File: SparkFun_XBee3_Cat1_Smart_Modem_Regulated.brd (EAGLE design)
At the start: 33 x 52.1 mm, 90 parts, among them J4 QWIIC_RIGHT_ANGLE, U2 AP63203

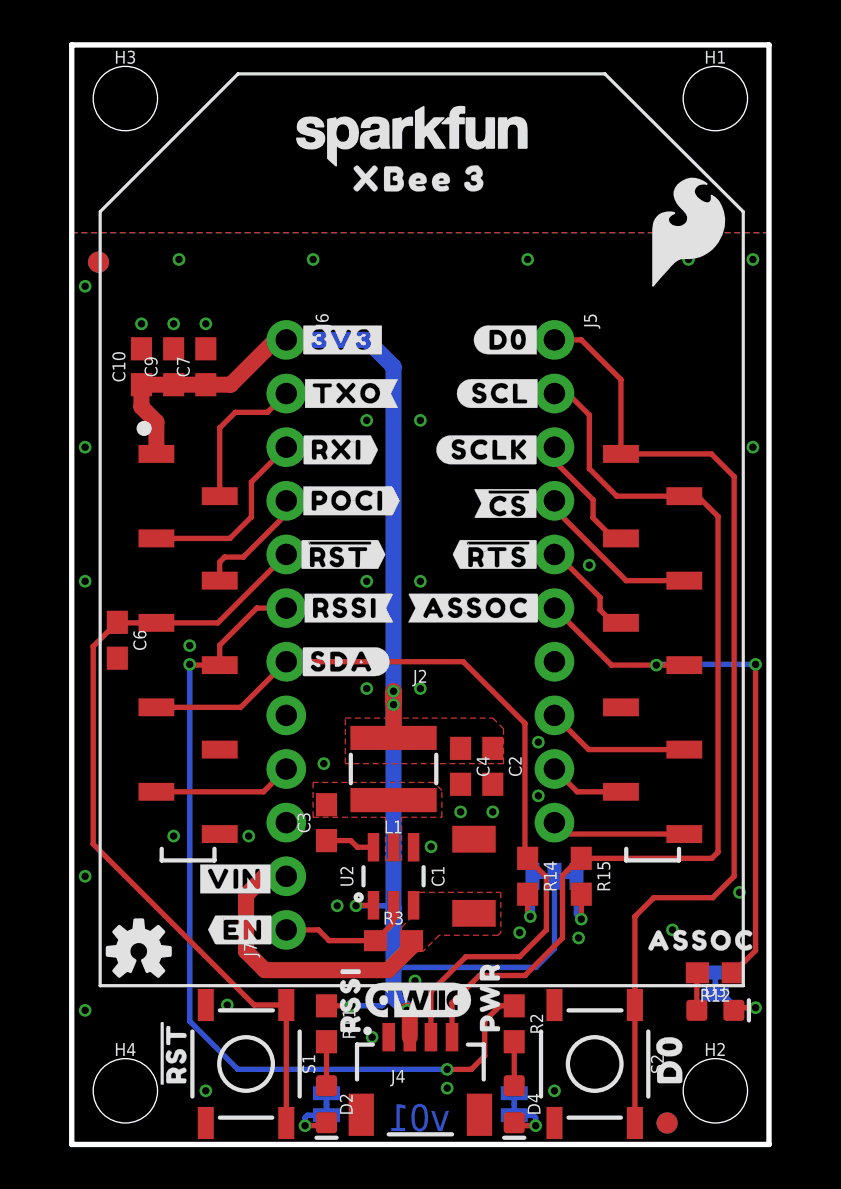
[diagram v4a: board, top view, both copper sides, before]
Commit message: Adds two additional layers, routes all nets, adds most silk
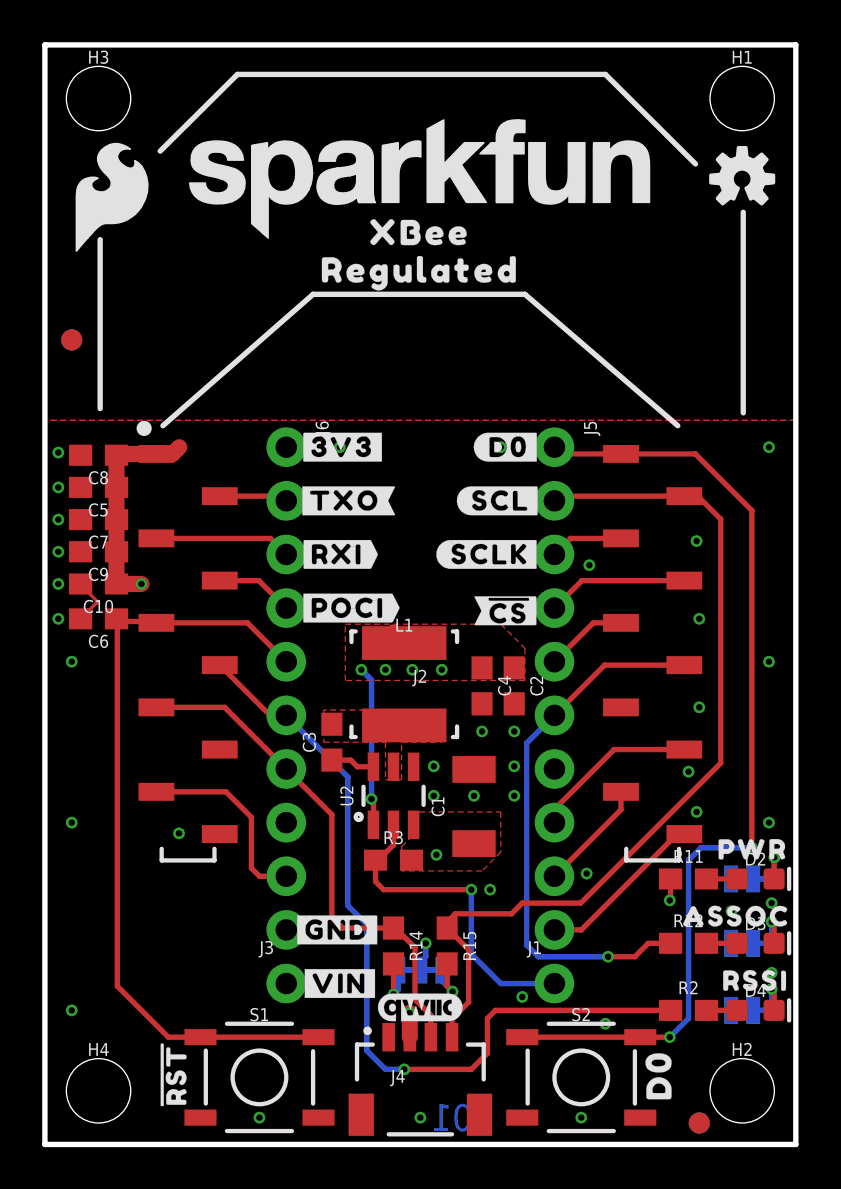
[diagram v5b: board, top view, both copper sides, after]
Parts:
- removed J7: (no value), SparkFun-Connectors:1X02_NO_SILK
- removed LOGO1: SFE_LOGO_NAME.1_INCH, SparkFun-Aesthetics:SFE_LOGO_NAME_.1
- removed U$37: (no value), topmirror:#D7##CTS##26
- removed U$38: (no value), topmirror:#D4#PICO#25
- removed U$48: (no value), topmirror:#EN#17
- removed U$51: (no value), topmirror:#RLED#22
- removed U$53: (no value), top:XBEE_335
- removed U$54: (no value), botmirror:##RST##13
- removed U$55: (no value), topmirror:#RSSI#16
- removed U$56: (no value), botmirror:#SDA#10
- removed U$57: (no value), botmirror:#ASSOC#28
- removed U$58: (no value), botmirror:##RTS##14
- removed U$67: (no value), botmirror:#EN#15
- added C5: 47pF, SparkFun-Capacitors:0603
- added C8: 10pF, SparkFun-Capacitors:0603
- added J1, J3: (no value), SparkFun-Connectors:1X01_NO_SILK_STAND
- added U$1: (no value), topmirror:#GND#0
- added U$10: (no value), top:#D4#PICO#25
- added U$2: (no value), SparkFun-Aesthetics:SFE_LOGO_NAME_.2
- added U$24, U$29: (no value), topmirror:REGULATED1343
- added U$25, U$28: (no value), top:XBEE340
- added U$3: (no value), topmirror:#EN#17
- added U$4: (no value), topmirror:#NC#1
- added U$5: (no value), botmirror:#NC#3
- added U$7: (no value), top:#D7##CTS##26
- D4: value BLUE -> Yellow
- J2: device xbee_smart_modem:XBEE3-SMD_SILK -> xbee_smart_modem:XBEE3-SMD
- L1: value 4.7μH -> 3.9UH; device SparkFun-Coils:INDUCTOR_4X4MM -> SparkFun-Coils:INDUCTOR_3.9UH
- LOGO3: value QWIIC_LOGO_5MM -> QWIIC_LOGO_4MM; device SparkFun-Aesthetics:QWIIC_5MM -> SparkFun-Aesthetics:QWIIC_4MM
- R11: value 1k -> 4.7k
- U$23: device top:XBEE_335 -> top:XBEE340
- moved LOGO2 46.4 mm to (31.8, 45.7)
- moved U$61 27.4 mm to (1.91, 44.8)
- moved D2 23.0 mm to (32.4, 12.6), turned to 0 degrees
- moved PLED 22.4 mm to (31.8, 12.6), turned to 180 degrees
- moved U$52 22.3 mm to (28.3, 12.6)
- moved U$62 19.2 mm to (32.4, 7.75), turned to 0 degrees
- moved R11 18.5 mm to (29.2, 12.6), turned to 0 degrees
- moved FRAME2 14.5 mm to (-10.2, -27.9)
- moved U$42 14.3 mm to (32.3, 14.0), turned to 0 degrees
- moved D4 12.3 mm to (32.4, 6.35), turned to 0 degrees
- moved RLED 11.7 mm to (31.8, 6.35), turned to 180 degrees
- moved C10 10.5 mm to (1.27, 26.5), turned to 180 degrees
- moved C9 9.46 mm to (1.27, 28.1), turned to 180 degrees
- moved C7 8.84 mm to (1.27, 29.6), turned to 180 degrees
- moved R2 8.28 mm to (29.2, 6.35), turned to 0 degrees
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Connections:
- net 3.3V: now also C5.1, C8.1
- net EN: now also J1.1; no longer J7.1
- net GND: now also C5.2, C8.2
- net VIN: now also J3.1; no longer J7.2
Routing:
- net 3.3V: track 69.3 -> 22.3 mm, vias 5 -> 9
- net D11/SDA: track 38.6 -> 24.5 mm
- net EN: track 6.47 -> 15.4 mm, vias 0 -> 1
- net VIN: track 13.9 -> 9.64 mm, vias 0 -> 1
- net D1/SCL: track 46.5 -> 42.7 mm
- net D13/TXO: track 7.06 -> 3.24 mm
- net D10/RSSI_PWM: track 41.7 -> 38.5 mm, vias 2 -> 1
- net D8/!DTR!: track 6.60 -> 9.22 mm
- net D14/RXI: track 8.91 -> 6.46 mm
- net GND: track 0.00 -> 2.41 mm, vias 41 -> 39
- net D2/SPI_CLK: track 5.83 -> 3.46 mm
- net D0: track 47.4 -> 45.5 mm, vias 0 -> 2
- net D7/!CTS!: track 3.60 -> 5.30 mm
- net D4/SPI_PICO: track 6.37 -> 8.03 mm
- net !RESET!: track 38.2 -> 36.8 mm
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- added copper zone on layer 15, net 3.3V
- added copper zone on layer 2, net GND
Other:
- board size 33 x 52.1 mm -> 35.6 x 52.1 mm

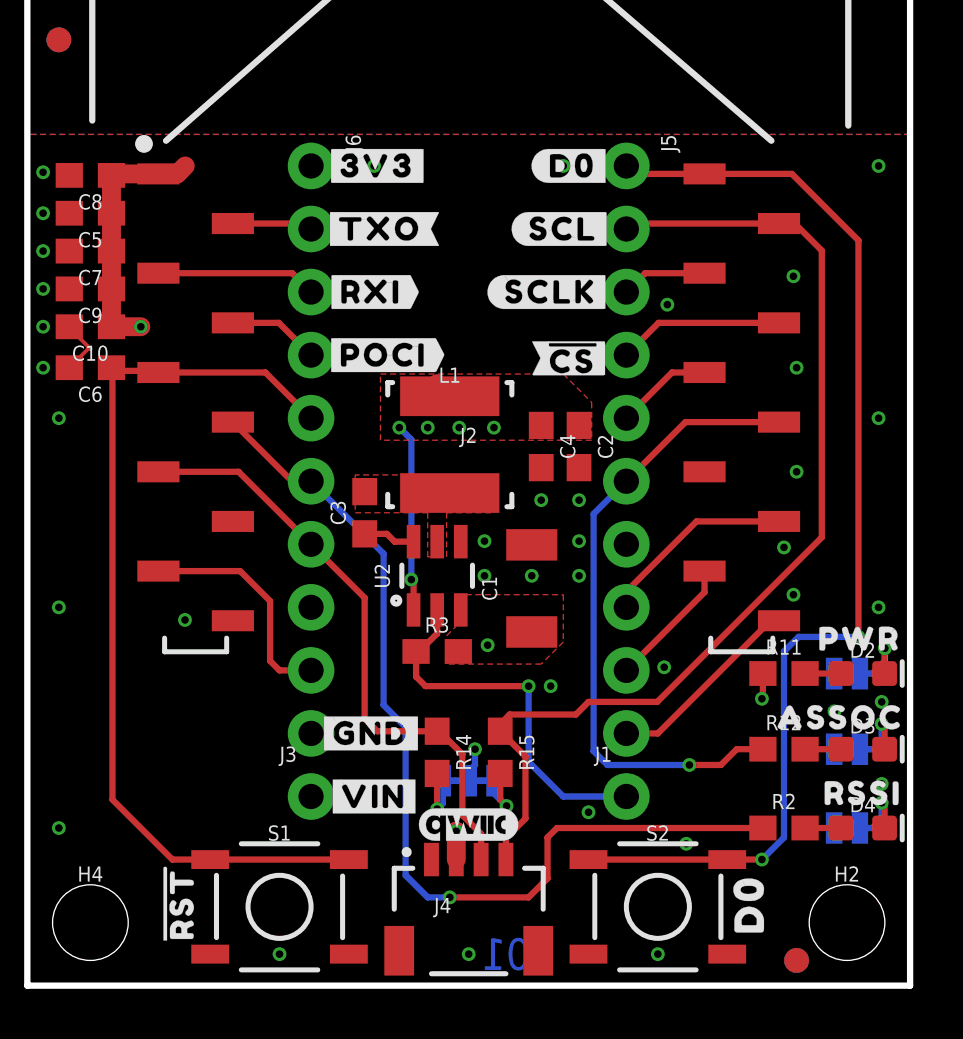
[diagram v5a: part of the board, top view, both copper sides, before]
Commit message: Adds more silk labels,  Adds ordering instructions
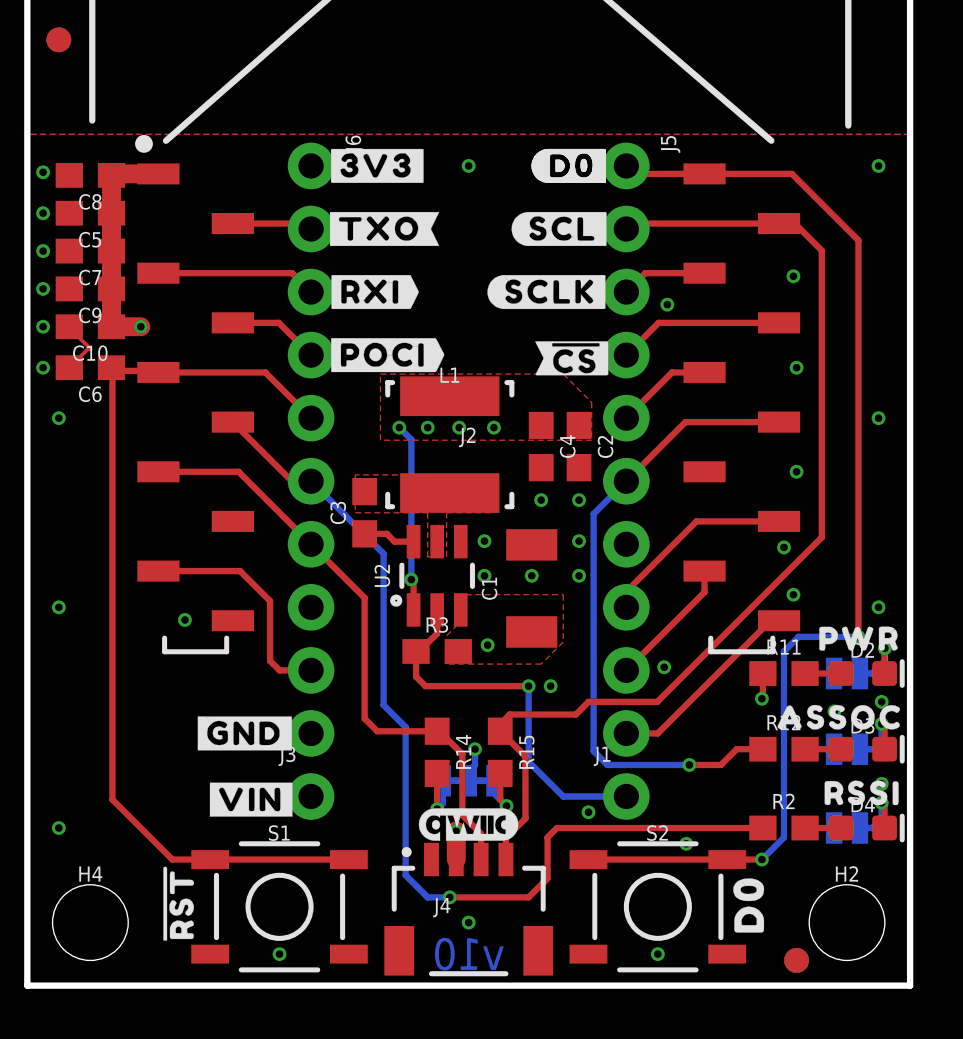
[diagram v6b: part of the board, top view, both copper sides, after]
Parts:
- removed U$6: (no value), topmirror:#D3#AD3#23
- added LOGO1: SPECIAL_INSTRUCTIONS-ORDERING, SparkFun-Aesthetics:ORDERING_INSTRUCTIONS
- added LOGO4: SFE_LOGO_NAMEBLANK, SparkFun-Aesthetics:BLANK
- added U$31: (no value), botmirror:#D0#3
- added U$32: (no value), topmirror:#D1#AD1#SCL#8
- added U$34: (no value), topmirror:#D3#AD3##CS##23
- U$11: device topmirror:#D1#AD1#8 -> topmirror:#RLED#22
- moved U$11 24.1 mm to (28.3, 6.35)
- moved U$1 5.08 mm to (7.49, 10.2)
- moved U$66 4.95 mm to (7.75, 7.49)
- moved U$59 0.13 mm to (20.8, 25.3)
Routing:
- net 3.3V: track 22.3 -> 20.3 mm
- net D12/SPI_POCI: track 4.27 -> 3.69 mm
- net GND: vias 39 -> 38
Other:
- board text added: "1.6mm Thickness"
- board text added: "Four Layer Board"
- board text added: "Lead Free HASL"
- board text added: "v10"
- board text removed: "v01"
